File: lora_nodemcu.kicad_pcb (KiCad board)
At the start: 4 copper layers, 25.8 x 32.9 mm, 17 parts, among them U1 RFM95, U2 LM1117-3.3, U3 WeMos_mini

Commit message: cleaned up footprint values and added BOM
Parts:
- C1, C2: value 10u -> 10uF
- C3: value C_Small -> 0.1uF
- C4, C5: value C_decoupling -> 0.1uF
- L1: value L_Core_Ferrite_Small -> 0k
- L2: value L_Core_Ferrite -> 0k
- R1: value 0k -> 0
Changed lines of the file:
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@@
-(kicad_pcb (version 20171130) (host pcbnew 5.0.0-rc2-dev-unknown-31e78d6~62~ubuntu17.10.1)
+(kicad_pcb (version 20171130) (host pcbnew 5.0.0-rc2-dev-unknown-f2bb398~62~ubuntu17.10.1)
   (general
     (thickness 1.2)
@@
     (36 B.SilkS user)
     (37 F.SilkS user)
-    (38 B.Mask user hide)
+    (38 B.Mask user)
     (39 F.Mask user hide)
     (40 Dwgs.User user)
@@
       (effects (font (size 1 1) (thickness 0.15)) (justify mirror))
     )
-    (fp_text value C_Small (at 0 -1.75 180) (layer B.Fab)
+    (fp_text value 0.1uF (at 0 -1.75 180) (layer B.Fab)
       (effects (font (size 1 1) (thickness 0.15)) (justify mirror))
     )
@@
       (effects (font (size 1 1) (thickness 0.15)) (justify mirror))
     )
-    (fp_text value C_decoupling (at 0 -1.75) (layer B.Fab)
+    (fp_text value 0.1uF (at 0 -1.75) (layer B.Fab)
       (effects (font (size 1 1) (thickness 0.15)) (justify mirror))
     )
@@
       (effects (font (size 1 1) (thickness 0.15)) (justify mirror))
     )
-    (fp_text value C_decoupling (at 0 -1.75 270) (layer B.Fab)
+    (fp_text value 0.1uF (at 0 -1.75 270) (layer B.Fab)
       (effects (font (size 1 1) (thickness 0.15)) (justify mirror))
     )
@@
       (effects (font (size 1 1) (thickness 0.15)) (justify mirror))
     )
-    (fp_text value L_Core_Ferrite (at 0 -2.1 270) (layer B.Fab)
+    (fp_text value 0k (at 0 -2.1 270) (layer B.Fab)
       (effects (font (size 1 1) (thickness 0.15)) (justify mirror))
     )
@@
       (effects (font (size 1 1) (thickness 0.15)) (justify mirror))
     )
-    (fp_text value L_Core_Ferrite_Small (at 0 -2.1) (layer B.Fab)
+    (fp_text value 0k (at 0 -2.1) (layer B.Fab)
       (effects (font (size 1 1) (thickness 0.15)) (justify mirror))
     )
@@
       (effects (font (size 1 1) (thickness 0.15)) (justify mirror))
     )
-    (fp_text value 10u (at 0 -1.75 270) (layer B.Fab)
+    (fp_text value 10uF (at 0 -1.75 270) (layer B.Fab)
       (effects (font (size 1 1) (thickness 0.15)) (justify mirror))
     )
@@
       (effects (font (size 1 1) (thickness 0.15)) (justify mirror))
     )
-    (fp_text value 10u (at 0 -1.75 270) (layer B.Fab)
+    (fp_text value 10uF (at 0 -1.75 270) (layer B.Fab)
       (effects (font (size 1 1) (thickness 0.15)) (justify mirror))
     )
@@
       (effects (font (size 1 1) (thickness 0.15)) (justify mirror))
     )
-    (fp_text value 0k (at 0 -1.75) (layer B.Fab)
-      (effects (font (size 1 1) (thickness 0.15)) (justify mirror))
-    )
+    (fp_text value 0 (at 0 -1.75) (layer B.Fab)
+      (effects (font (size 1 1) (thickness 0.15)) (justify mirror))
+    )

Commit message: connects two lines on schematic that I missed in last commit
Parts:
- L1, L2, R2, R3, R4, R5, R6: value 0k -> JUMPER
- R1: value 0 -> JUMPER
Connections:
- R5 pad 1: /MISO -> Net-(R5-Pad1)
- R6 pad 1: /MOSI -> Net-(R6-Pad1)
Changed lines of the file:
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@@
-(kicad_pcb (version 20171130) (host pcbnew 5.0.0-rc2-dev-unknown-f2bb398~62~ubuntu17.10.1)
+(kicad_pcb (version 20171130) (host pcbnew 5.0.0-rc2-dev-unknown-c6ef0d5~62~ubuntu17.10.1)
   (general
     (thickness 1.2)
@@
     (zones 0)
     (modules 17)
-    (nets 32)
+    (nets 34)
   )
   (page A4)
@@
   (net 30 /wemos_5V)
   (net 31 /RF95_3V3)
+  (net 32 "Net-(R6-Pad1)")
+  (net 33 "Net-(R5-Pad1)")
   (net_class Default "This is the default net class."
     (clearance 0.2)
@@
     (add_net "Net-(R3-Pad2)")
     (add_net "Net-(R4-Pad2)")
+    (add_net "Net-(R5-Pad1)")
     (add_net "Net-(R5-Pad2)")
+    (add_net "Net-(R6-Pad1)")
     (add_net "Net-(R6-Pad2)")
     (add_net "Net-(U1-Pad11)")
@@
       (effects (font (size 1 1) (thickness 0.15)) (justify mirror))
     )
-    (fp_text value 0k (at 0 -2.1 270) (layer B.Fab)
+    (fp_text value JUMPER (at 0 -2.1 270) (layer B.Fab)
       (effects (font (size 1 1) (thickness 0.15)) (justify mirror))
     )
@@
       (effects (font (size 1 1) (thickness 0.15)) (justify mirror))
     )
-    (fp_text value 0k (at 0 -2.1) (layer B.Fab)
+    (fp_text value JUMPER (at 0 -2.1) (layer B.Fab)
       (effects (font (size 1 1) (thickness 0.15)) (justify mirror))
     )
@@
       (effects (font (size 1 1) (thickness 0.15)) (justify mirror))
     )
-    (fp_text value 0 (at 0 -1.75) (layer B.Fab)
+    (fp_text value JUMPER (at 0 -1.75) (layer B.Fab)
       (effects (font (size 1 1) (thickness 0.15)) (justify mirror))
     )
@@
       (effects (font (size 1 1) (thickness 0.15)) (justify mirror))
     )
-    (fp_text value 0k (at 0 -1.75) (layer B.Fab)
+    (fp_text value JUMPER (at 0 -1.75) (layer B.Fab)
       (effects (font (size 1 1) (thickness 0.15)) (justify mirror))
     )
@@
       (effects (font (size 1 1) (thickness 0.15)) (justify mirror))
     )
-    (fp_text value 0k (at 0 -1.75 180) (layer B.Fab)
+    (fp_text value JUMPER (at 0 -1.75 180) (layer B.Fab)
       (effects (font (size 1 1) (thickness 0.15)) (justify mirror))
     )
@@
       (effects (font (size 1 1) (thickness 0.15)) (justify mirror))
     )
-    (fp_text value 0k (at 0 -1.75 180) (layer B.Fab)
+    (fp_text value JUMPER (at 0 -1.75 180) (layer B.Fab)
       (effects (font (size 1 1) (thickness 0.15)) (justify mirror))
     )
@@
       (effects (font (size 1 1) (thickness 0.15)) (justify mirror))
     )
-    (fp_text value 0k (at 0 -1.75 180) (layer B.Fab)
+    (fp_text value JUMPER (at 0 -1.75 180) (layer B.Fab)
       (effects (font (size 1 1) (thickness 0.15)) (justify mirror))
     )
@@
     (fp_line (start 2.35 -0.9) (end -2.35 -0.9) (layer B.CrtYd) (width 0.05))
     (pad 1 smd rect (at -1.35 0 180) (size 1.5 1.3) (layers B.Cu B.Mask)
-      (net 9 /MISO))
+      (net 33 "Net-(R5-Pad1)"))
     (pad 2 smd rect (at 1.35 0 180) (size 1.5 1.3) (layers B.Cu B.Mask)
       (net 10 "Net-(R5-Pad2)"))
@@
       (effects (font (size 1 1) (thickness 0.15)) (justify mirror))
     )
-    (fp_text value 0k (at 0 -1.75 180) (layer B.Fab)
+    (fp_text value JUMPER (at 0 -1.75 180) (layer B.Fab)
       (effects (font (size 1 1) (thickness 0.15)) (justify mirror))
     )
@@
     (fp_line (start 2.35 -0.9) (end -2.35 -0.9) (layer B.CrtYd) (width 0.05))
     (pad 1 smd rect (at -1.35 0 180) (size 1.5 1.3) (layers B.Cu B.Mask)
-      (net 11 /MOSI))
+      (net 32 "Net-(R6-Pad1)"))
     (pad 2 smd rect (at 1.35 0 180) (size 1.5 1.3) (layers B.Cu B.Mask)
       (net 12 "Net-(R6-Pad2)"))

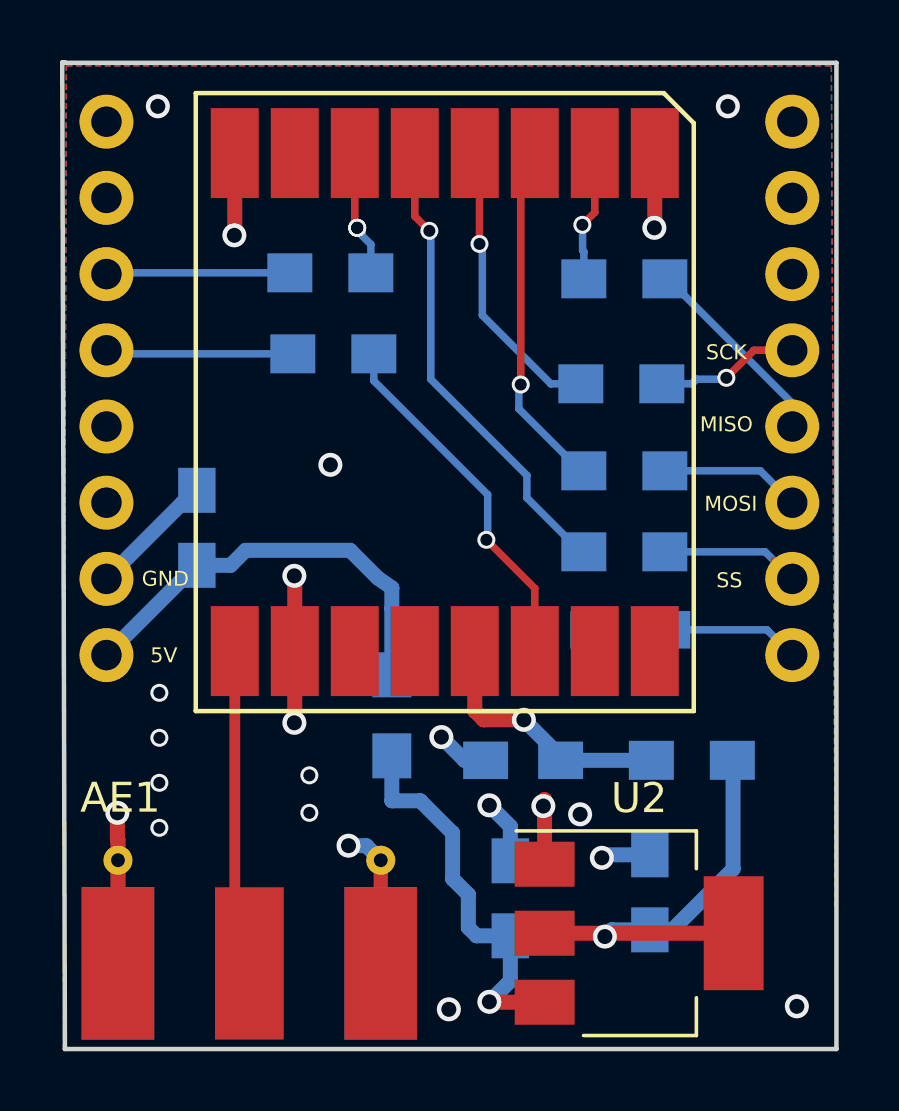
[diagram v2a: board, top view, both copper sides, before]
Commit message: changes jumper resistors to bridged solder points
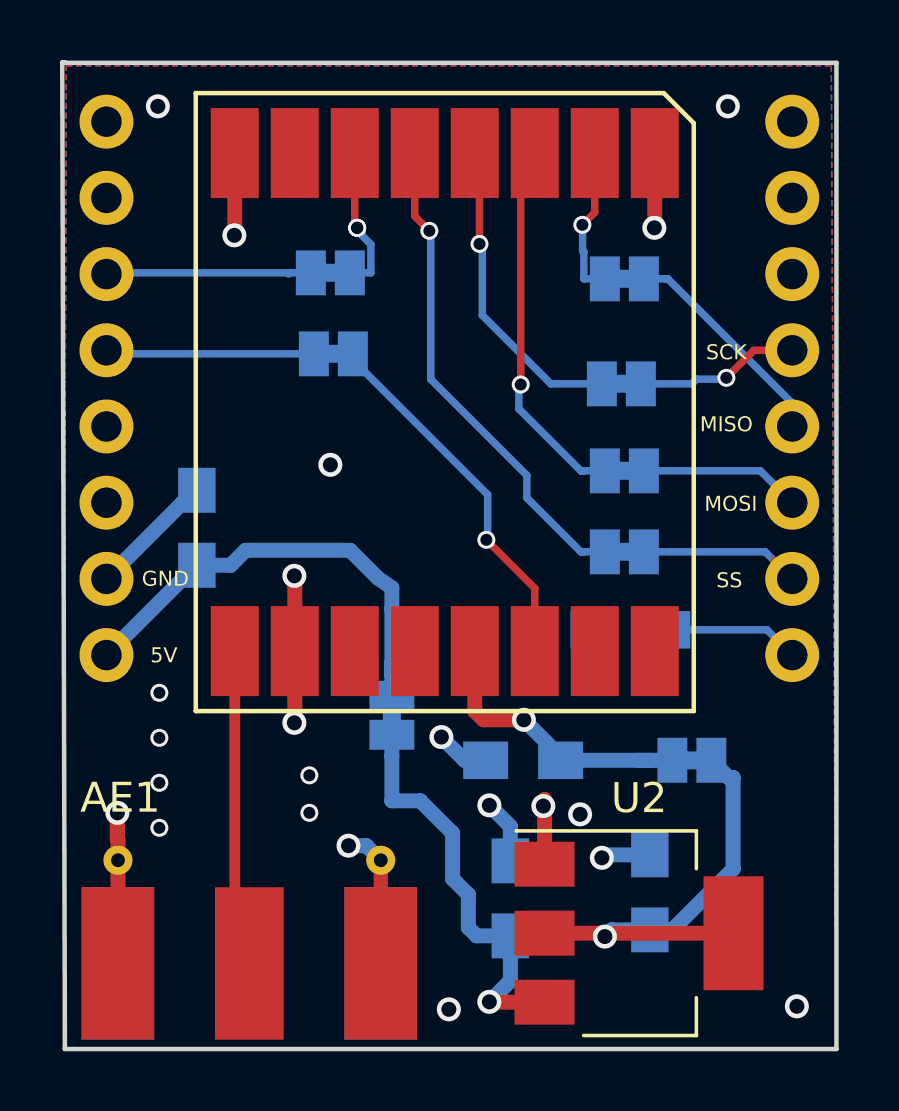
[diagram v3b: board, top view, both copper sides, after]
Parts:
- L1, L2: footprint Inductors_SMD:L_0805_HandSoldering -> Jumper:SolderJumper-2_P1.3mm_Bridged_Pad1.0x1.5mm
- R1, R2, R3, R4, R5, R6: footprint Resistors_SMD:R_0805_HandSoldering -> Jumper:SolderJumper-2_P1.3mm_Bridged_Pad1.0x1.5mm
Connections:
- R5 pad 1: Net-(R5-Pad1) -> /MISO
- R6 pad 1: Net-(R6-Pad1) -> /MOSI
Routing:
- net /RF95_3V3: track 8.64 -> 10.1 mm
- net /MISO: track 6.74 -> 8.01 mm
- net Net-(R2-Pad1): track 6.19 -> 7.37 mm
- net Net-(R1-Pad1): track 6.26 -> 7.44 mm
- net /SCK: track 4.81 -> 5.98 mm
- net /SS: track 5.47 -> 6.65 mm
- net /MOSI: track 4.69 -> 5.86 mm
- net /wemos_5V: track 13.7 -> 14.8 mm
- net +3V3: track 14.6 -> 15.5 mm
- net Net-(R3-Pad2): track 15.7 -> 16.5 mm
- net Net-(R6-Pad2): track 11.8 -> 12.6 mm
- net Net-(R2-Pad2): track 4.21 -> 4.91 mm
- net Net-(R5-Pad2): track 4.38 -> 5.08 mm
- net Net-(R4-Pad2): track 9.74 -> 10.4 mm
- net +5V: track 13.2 -> 13.8 mm
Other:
- board text added: "D2"
- board text added: "Disaster Radio V0.3 180319"
- board text added: "RESET"
- board text removed: "Disaster Radio V0.2 180109"
